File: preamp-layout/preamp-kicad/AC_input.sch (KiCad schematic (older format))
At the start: 7 parts, among them J1 Conn_01x02_Female, J2 Screw_Terminal_01x03, J3 Screw_Terminal_01x03, J4 Screw_Terminal_01x03

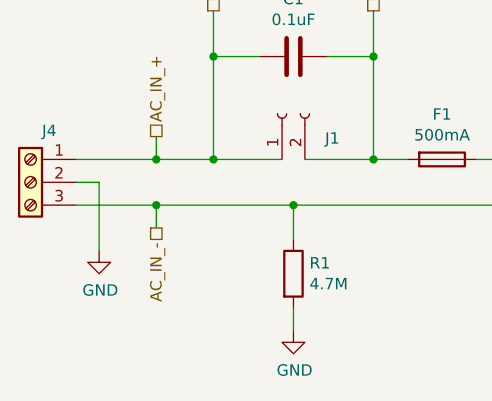
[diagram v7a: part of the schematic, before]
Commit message: AC ground conn update
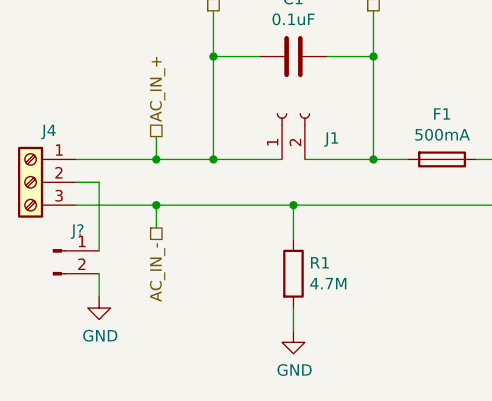
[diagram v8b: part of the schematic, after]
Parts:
- added J?: Conn_01x02_Male, Connector_JST:JST_EH_B2B-EH-A_1x02_P2.50mm_Vertical, symbol Connector:Conn_01x02_Male
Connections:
- net GND: now also J?.2 (Pin_2); no longer J4.2 (Pin_2)
- new net: J4.2 (Pin_2), J?.1 (Pin_1)
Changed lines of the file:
@@
 	5450 4500 5450 4600
 Wire Wire Line
-	6750 3250 7150 3250
-Wire Wire Line
 	6250 3850 6550 3850
-Wire Wire Line
-	6900 3450 7150 3450
 Wire Wire Line
 	5450 4050 6550 4050
 Wire Wire Line
 	6550 3750 6550 3850
-Connection ~ 6550 3850
-Wire Wire Line
-	6550 3850 6750 3850
 Wire Wire Line
 	6550 4150 6550 4050
-Connection ~ 6550 4050
-Wire Wire Line
-	6550 4050 6900 4050
 Text HLabel 5100 3200 1    50   UnSpc ~ 0
 PWR_SW_1
@@
 Text HLabel 4850 4150 3    50   UnSpc ~ 0
 AC_IN_-
-Connection ~ 6750 3850
-Wire Wire Line
-	6900 4650 7150 4650
 Wire Wire Line
 	4850 3750 4850 3850
@@
 	-1   0    0    -1
 $EndComp
+Wire Wire Line
+	4500 4050 4850 4050
+Wire Wire Line
+	4500 3850 4850 3850
+Wire Wire Line
+	4500 3950 4600 3950
+Wire Wire Line
+	4600 3950 4600 4250
+Connection ~ 4850 4050
+Wire Wire Line
+	4850 4050 5450 4050
+Connection ~ 4850 3850
+Wire Wire Line
+	4850 3850 5100 3850
 $Comp
-L Connector:Screw_Terminal_01x03 J2
-U 1 1 5E8BEBC3
-P 7350 3350
-F 0 "J2" H 7430 3346 50  0000 L CNN
-F 1 "Screw_Terminal_01x03" H 7268 3116 50  0001 C CNN
-F 2 "TerminalBlock_Phoenix:TerminalBlock_Phoenix_MKDS-3-3-5.08_1x03_P5.08mm_Horizontal" H 7350 3350 50  0001 C CNN
-F 3 "~" H 7350 3350 50  0001 C CNN
-	1    7350 3350
+L Connector:Conn_01x02_Male J?
+U 1 1 5F12D3AA
+P 4400 4250
+AR Path="/5E5EF2D4/5F12D3AA" Ref="J?"  Part="1"
+AR Path="/5E26F6FE/5F12D3AA" Ref="J?"  Part="1"
+F 0 "J?" H 4508 4339 50  0000 C CNN
+F 1 "Conn_01x02_Male" H 4372 4133 50  0001 R CNN
+F 2 "Connector_JST:JST_EH_B2B-EH-A_1x02_P2.50mm_Vertical" H 4400 4250 50  0001 C CNN
+F 3 "~" H 4400 4250 50  0001 C CNN
+	1    4400 4250
 	1    0    0    -1
 $EndComp
 $Comp
-L Connector:Screw_Terminal_01x03 J3
-U 1 1 5E8C1BA2
-P 7350 4550
-F 0 "J3" H 7430 4546 50  0000 L CNN
-F 1 "Screw_Terminal_01x03" H 7268 4316 50  0001 C CNN
-F 2 "TerminalBlock_Phoenix:TerminalBlock_Phoenix_MKDS-3-3-5.08_1x03_P5.08mm_Horizontal" H 7350 4550 50  0001 C CNN
-F 3 "~" H 7350 4550 50  0001 C CNN
-	1    7350 4550
+L power:GND #PWR0111
+U 1 1 5E8D595F
+P 4600 4450
+F 0 "#PWR0111" H 4600 4200 50  0001 C CNN
+F 1 "GND" H 4605 4277 50  0000 C CNN
+F 2 "" H 4600 4450 50  0001 C CNN
+F 3 "" H 4600 4450 50  0001 C CNN
+	1    4600 4450
 	1    0    0    -1
 $EndComp
+Connection ~ 6550 4050
+Connection ~ 6550 3850
 Wire Wire Line
-	7150 3350 7050 3350
+	7050 3850 7050 4550
 Wire Wire Line
-	7050 4550 7150 4550
+	6750 3850 6750 4450
+Connection ~ 6900 4050
+Wire Wire Line
+	6900 4050 6900 4650
+Wire Wire Line
+	6750 4450 7150 4450
+Wire Wire Line
+	7050 3350 7050 3850
+Wire Wire Line
+	6900 3450 6900 4050
+Wire Wire Line
+	6750 3250 6750 3850
+Connection ~ 7050 3850
+Wire Wire Line
+	7200 3850 7050 3850
+Wire Wire Line
+	7200 3900 7200 3850
 $Comp
 L power:GND #PWR0110
@@
 $EndComp
 Wire Wire Line
-	7200 3900 7200 3850
+	7050 4550 7150 4550
 Wire Wire Line
-	7200 3850 7050 3850
-Connection ~ 7050 3850
-Wire Wire Line
-	6750 3250 6750 3850
-Wire Wire Line
-	6900 3450 6900 4050
-Wire Wire Line
-	7050 3350 7050 3850
-Wire Wire Line
-	6750 4450 7150 4450
-Wire Wire Line
-	6900 4050 6900 4650
-Connection ~ 6900 4050
-Wire Wire Line
-	6750 3850 6750 4450
-Wire Wire Line
-	7050 3850 7050 4550
-Wire Wire Line
-	4500 4050 4850 4050
-Wire Wire Line
-	4500 3850 4850 3850
+	7150 3350 7050 3350
 $Comp
-L power:GND #PWR0111
-U 1 1 5E8D595F
-P 4600 4250
-F 0 "#PWR0111" H 4600 4000 50  0001 C CNN
-F 1 "GND" H 4605 4077 50  0000 C CNN
-F 2 "" H 4600 4250 50  0001 C CNN
-F 3 "" H 4600 4250 50  0001 C CNN
-	1    4600 4250
+L Connector:Screw_Terminal_01x03 J3
+U 1 1 5E8C1BA2
+P 7350 4550
+F 0 "J3" H 7430 4546 50  0000 L CNN
+F 1 "Screw_Terminal_01x03" H 7268 4316 50  0001 C CNN
+F 2 "TerminalBlock_Phoenix:TerminalBlock_Phoenix_MKDS-3-3-5.08_1x03_P5.08mm_Horizontal" H 7350 4550 50  0001 C CNN
+F 3 "~" H 7350 4550 50  0001 C CNN
+	1    7350 4550
+	1    0    0    -1
+$EndComp
+$Comp
+L Connector:Screw_Terminal_01x03 J2
+U 1 1 5E8BEBC3
+P 7350 3350
+F 0 "J2" H 7430 3346 50  0000 L CNN
+F 1 "Screw_Terminal_01x03" H 7268 3116 50  0001 C CNN
+F 2 "TerminalBlock_Phoenix:TerminalBlock_Phoenix_MKDS-3-3-5.08_1x03_P5.08mm_Horizontal" H 7350 3350 50  0001 C CNN
+F 3 "~" H 7350 3350 50  0001 C CNN
+	1    7350 3350
 	1    0    0    -1
 $EndComp
 Wire Wire Line
-	4500 3950 4600 3950
+	6900 4650 7150 4650
+Connection ~ 6750 3850
 Wire Wire Line
-	4600 3950 4600 4250
-Connection ~ 4850 4050
+	6550 4050 6900 4050
 Wire Wire Line
-	4850 4050 5450 4050
-Connection ~ 4850 3850
+	6550 3850 6750 3850
 Wire Wire Line
-	4850 3850 5100 3850
+	6900 3450 7150 3450
+Wire Wire Line
+	6750 3250 7150 3250
+Wire Wire Line
+	4600 4350 4600 4450
 $EndSCHEMATC
